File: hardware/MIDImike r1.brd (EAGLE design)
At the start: 84.8 x 53.3 mm, 7 parts, among them SW1 PUSH-BTN

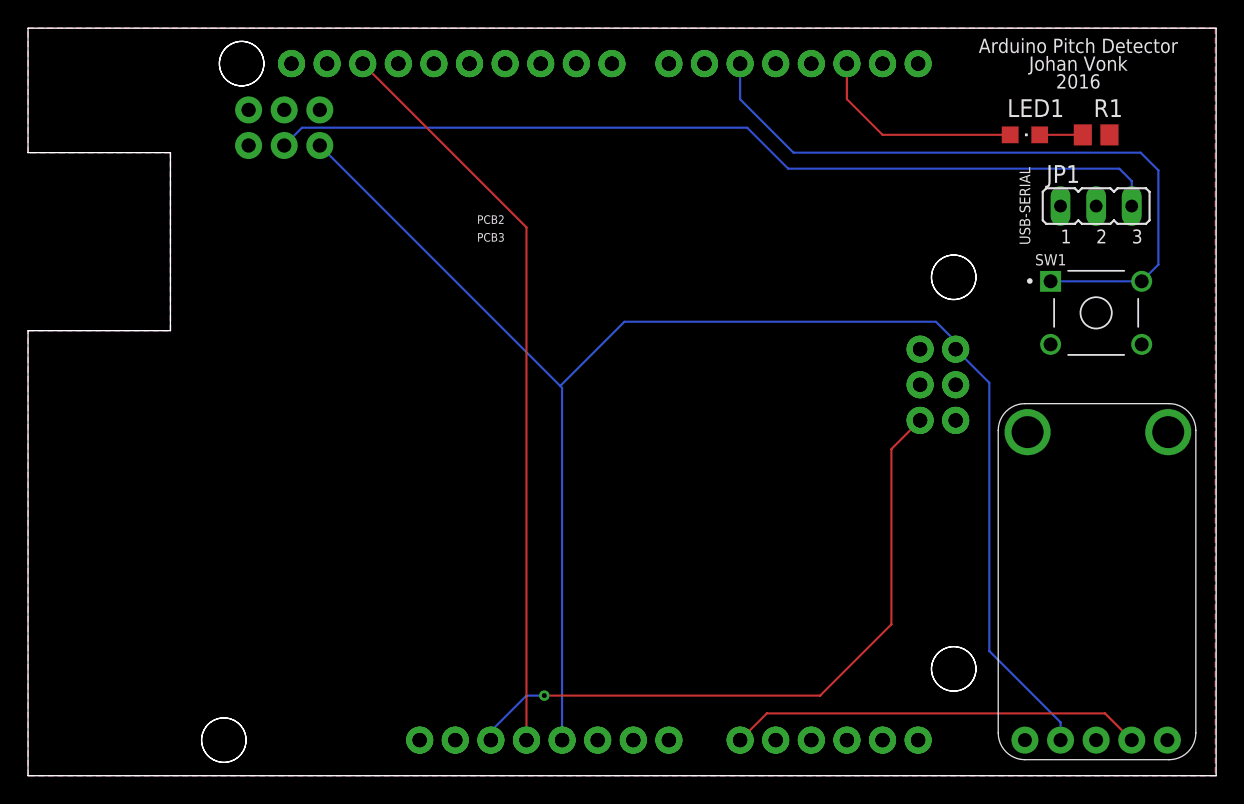
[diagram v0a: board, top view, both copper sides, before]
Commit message: add rotary dip switch to allow for pitch shift
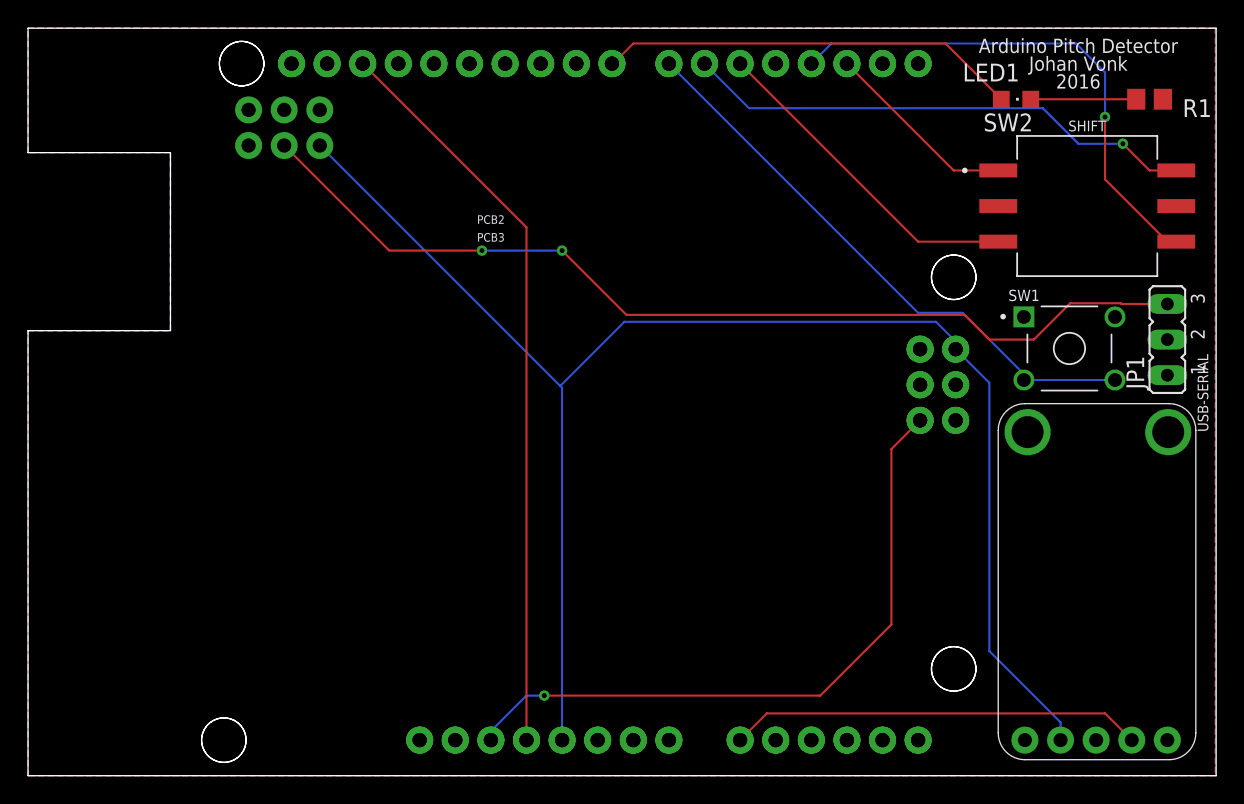
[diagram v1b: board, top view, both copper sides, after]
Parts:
- added SW2: SH-7030TB, Coert-Vonk:SW_RDS-16S-1045-SMT-TR
- moved JP1 10.8 mm to (81.3, 31.1), turned to 90 degrees
- moved R1 4.58 mm to (80.0, 48.3)
- moved SW1 3.18 mm to (74.3, 30.5)
- moved LED1 2.62 mm to (70.5, 48.3)
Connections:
- removed net REPLAY: PCB2.D5, SW1.1, SW1.1@1
- new net D7: PCB2.D7, SW1.2, SW1.2@1
- new net D8: LED1.A, PCB2.D8
- new net N$10: PCB2.D3, SW2.2
- new net N$13: PCB2.D5, SW2.4
- new net N$14: PCB2.D6, SW2.8
- net GND: now also SW1.1, SW1.1@1, SW2.C_1, SW2.C_2; no longer SW1.2, SW1.2@1
- net N$1: now also SW2.1; no longer LED1.A
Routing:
- net REPLAY: track 49.4 -> 0.00 mm
- net D7: track 0.00 -> 41.4 mm
- net N$10: track 0.00 -> 37.0 mm, vias 0 -> 1
- net N$14: track 0.00 -> 36.8 mm, vias 0 -> 1
- net D8: track 0.00 -> 30.0 mm
- net N$13: track 0.00 -> 23.7 mm
- net N$3: track 64.3 -> 69.8 mm, vias 0 -> 2
- net N$8: track 3.08 -> 7.53 mm
- net N$1: track 15.2 -> 14.0 mm
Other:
- board text added: "SHIFT"
